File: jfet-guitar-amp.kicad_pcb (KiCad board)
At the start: 2 copper layers, 78 x 21 mm, 51 parts, among them J1 Conn_2, J2 Conn_2, J3 AudioJack4, Q1 J201, Q2 J201, Q3 J201, U1 4580, U2 TSX9291

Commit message: prepare to send to manufacture
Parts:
- R21, R22: value 4K7 -> NF
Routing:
- net Net-(C4-Pad1): track 16.2 -> 18.3 mm
- net /V_Gnd: track 88.9 -> 89.5 mm
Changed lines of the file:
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@@
-(kicad_pcb (version 20171130) (host pcbnew "(5.0.2)-1")
+(kicad_pcb (version 20171130) (host pcbnew 5.0.2-bee76a0~70~ubuntu18.04.1)
   (general
     (thickness 1.6)
     (drawings 16)
-    (tracks 185)
+    (tracks 189)
     (zones 0)
     (modules 51)
@@
   )
   (setup
-    (last_trace_width 0.5)
+    (last_trace_width 0.25)
     (user_trace_width 0.5)
     (trace_clearance 0.2)
@@
       (effects (font (size 1 1) (thickness 0.15)))
     )
-    (fp_text value 4K7 (at 0 1.65 180) (layer F.Fab)
+    (fp_text value NF (at 0 1.65 180) (layer F.Fab)
       (effects (font (size 1 1) (thickness 0.15)))
     )
@@
       (effects (font (size 1 1) (thickness 0.15)))
     )
-    (fp_text value 4K7 (at 0 1.65 180) (layer F.Fab)
+    (fp_text value NF (at 0 1.65 180) (layer F.Fab)
       (effects (font (size 1 1) (thickness 0.15)))
     )
@@
   (segment (start 112.76 94.168) (end 112.76 95.9175) (width 0.5) (layer F.Cu) (net 3))
   (segment (start 89.9645 94.615) (end 91.6455 94.615) (width 0.5) (layer F.Cu) (net 4))
-  (segment (start 96.3065 89.154) (end 103.415208 89.154) (width 0.5) (layer F.Cu) (net 4))
-  (segment (start 91.6455 93.815) (end 96.3065 89.154) (width 0.5) (layer F.Cu) (net 4))
-  (segment (start 91.6455 94.615) (end 91.6455 93.815) (width 0.5) (layer F.Cu) (net 4))
+  (segment (start 91.6455 94.615) (end 91.6455 90.2185) (width 0.5) (layer F.Cu) (net 4))
+  (segment (start 92.71 89.154) (end 103.415208 89.154) (width 0.5) (layer F.Cu) (net 4))
+  (segment (start 91.6455 90.2185) (end 92.71 89.154) (width 0.5) (layer F.Cu) (net 4))
   (segment (start 87.9575 94.483) (end 88.0895 94.615) (width 0.5) (layer F.Cu) (net 5))
   (segment (start 86.471 94.483) (end 87.9575 94.483) (width 0.5) (layer F.Cu) (net 5))
@@
   (segment (start 74.5975 89.154) (end 74.5975 91.186) (width 0.5) (layer F.Cu) (net 9))
   (segment (start 74.4705 91.313) (end 76.1515 91.313) (width 0.5) (layer F.Cu) (net 9))
-  (segment (start 87.46 102.573) (end 87.46 102.804) (width 0.25) (layer F.Cu) (net 10))
-  (segment (start 85.26 100.904) (end 85.791 100.904) (width 0.25) (layer F.Cu) (net 10))
-  (segment (start 85.791 100.904) (end 87.46 102.573) (width 0.25) (layer F.Cu) (net 10))
   (segment (start 105.1165 100.711) (end 100.3695 100.711) (width 0.5) (layer F.Cu) (net 10))
   (segment (start 100.3695 102.1955) (end 100.3695 100.711) (width 0.5) (layer F.Cu) (net 10))
@@
   (segment (start 138.811 102.489) (end 138.684 102.616) (width 0.5) (layer B.Cu) (net 10))
   (segment (start 134.874 102.616) (end 133.096 102.616) (width 0.5) (layer B.Cu) (net 10))
+  (segment (start 87.46 102.024) (end 87.46 102.804) (width 0.25) (layer F.Cu) (net 10))
+  (segment (start 86.172 100.904) (end 86.36 101.092) (width 0.25) (layer F.Cu) (net 10))
+  (segment (start 86.36 101.092) (end 86.36 101.6) (width 0.25) (layer F.Cu) (net 10))
+  (segment (start 86.36 101.6) (end 86.614 101.854) (width 0.25) (layer F.Cu) (net 10))
+  (segment (start 85.26 100.904) (end 86.172 100.904) (width 0.25) (layer F.Cu) (net 10))
+  (segment (start 86.614 101.854) (end 87.29 101.854) (width 0.25) (layer F.Cu) (net 10))
+  (segment (start 87.29 101.854) (end 87.46 102.024) (width 0.25) (layer F.Cu) (net 10))
   (segment (start 109.0145 93.218) (end 109.0145 95.25) (width 0.5) (layer F.Cu) (net 11))
   (segment (start 109.0145 93.218) (end 110.76 93.218) (width 0.5) (layer F.Cu) (net 11))

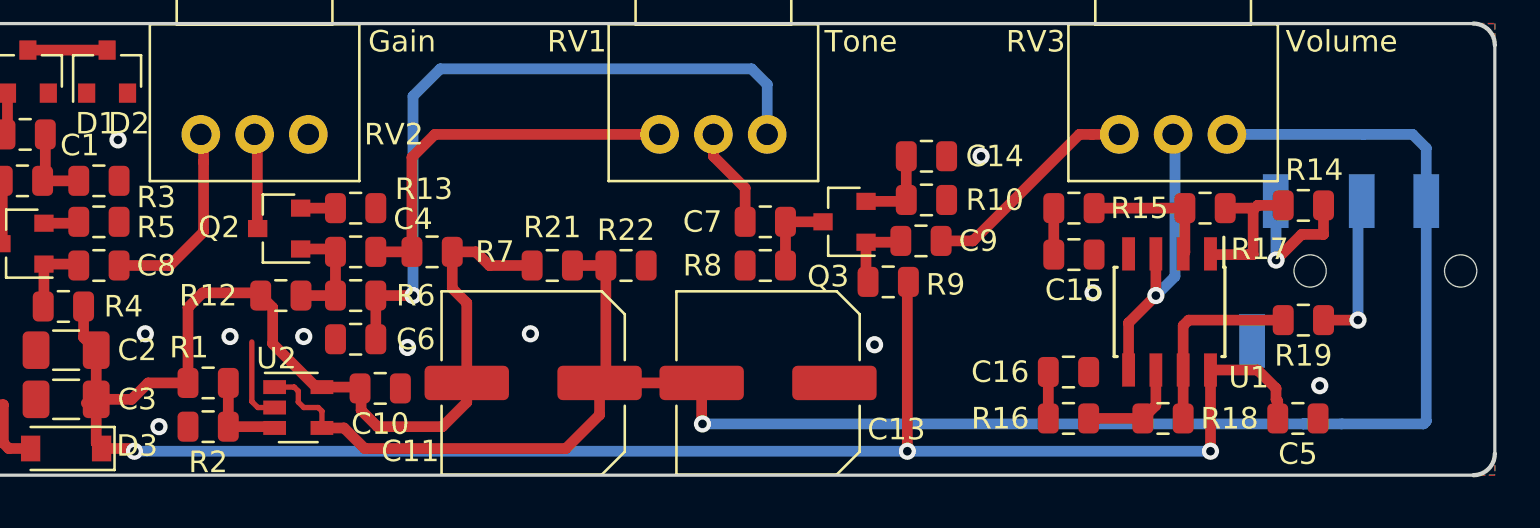
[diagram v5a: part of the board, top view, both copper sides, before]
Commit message: minor schematic changes to feedback loop and BOM, tag for prototype production
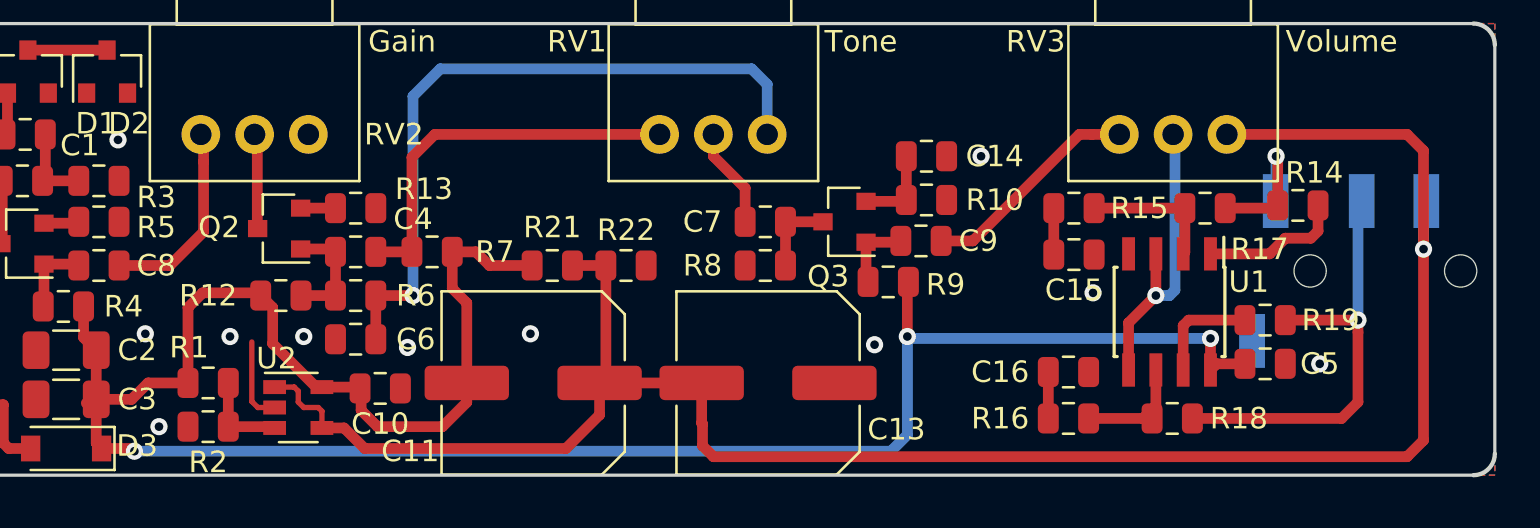
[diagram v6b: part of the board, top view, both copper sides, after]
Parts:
- C11, C13: value 470u -> NF
- moved C5 2.96 mm to (131.3, 99.8)
- moved R19 1.78 mm to (131.3, 97.8)
- moved R18 0.43 mm to (127.0, 102.4)
- moved R14 0.25 mm to (132.8, 92.5), turned to 180 degrees
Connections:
- R17 pad 1: Net-(R14-Pad1) -> Net-(J3-PadT)
- R18 pad 1: Net-(R18-Pad1) -> Net-(J3-PadR1)
- R19 pad 2: Net-(R18-Pad1) -> Net-(R19-Pad2)
- U1 pad 7: Net-(R18-Pad1) -> Net-(R19-Pad2)
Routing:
- net Net-(J3-PadR1): track 7.21 -> 20.8 mm
- net Net-(R18-Pad1): track 9.07 -> 0.00 mm
- net +9V: track 112.8 -> 107.0 mm
- net Net-(R19-Pad2): track 0.00 -> 5.04 mm
- net /V_Gnd: track 89.5 -> 93.6 mm
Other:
- board text added: "JFET guitar headphone amp Designed by Joe Earlam Rev 2"
- board text removed: "JFET guitar headphone amp Designed by Joe Earlam Rev2"

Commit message: as sent to production
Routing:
- net Net-(RV3-Pad2): track 14.2 -> 25.3 mm, vias 1 -> 0
- net Net-(C9-Pad1): track 10.3 -> 11.9 mm
- net GND: vias 12 -> 13
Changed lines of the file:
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@@
-(kicad_pcb (version 20171130) (host pcbnew 5.0.2-bee76a0~70~ubuntu16.04.1)
+(kicad_pcb (version 20171130) (host pcbnew 5.0.2-bee76a0~70~ubuntu18.04.1)
   (general
     (thickness 1.6)
     (drawings 16)
-    (tracks 195)
+    (tracks 202)
     (zones 0)
     (modules 51)
@@
       (drillshape 0)
       (scaleselection 1)
-      (outputdirectory "../../../../gerbers/jfet/"))
+      (outputdirectory "/home/joe/gerbers/jfet/"))
   )
   (net 0 "")
@@
   (via (at 79.248 98.425) (size 0.8) (drill 0.4) (layers F.Cu B.Cu) (net 8))
   (via (at 133.858 99.822) (size 0.8) (drill 0.4) (layers F.Cu B.Cu) (net 8))
+  (via (at 119.761 100.076) (size 0.8) (drill 0.4) (layers F.Cu B.Cu) (net 8))
   (segment (start 74.5975 91.186) (end 74.4705 91.313) (width 0.5) (layer F.Cu) (net 9))
   (segment (start 74.5975 89.154) (end 74.5975 91.186) (width 0.5) (layer F.Cu) (net 9))
@@
   (segment (start 72.898 103.759) (end 73.915 103.759) (width 0.5) (layer F.Cu) (net 13))
   (segment (start 72.644 103.505) (end 72.898 103.759) (width 0.5) (layer F.Cu) (net 13))
-  (segment (start 123.267208 89.154) (end 124.54 89.154) (width 0.5) (layer F.Cu) (net 14))
-  (segment (start 122.682 89.154) (end 123.267208 89.154) (width 0.5) (layer F.Cu) (net 14))
-  (segment (start 116.2535 94.107) (end 117.729 94.107) (width 0.5) (layer F.Cu) (net 14))
-  (segment (start 117.729 94.107) (end 122.682 89.154) (width 0.5) (layer F.Cu) (net 14))
+  (segment (start 118.960001 92.875999) (end 117.729 94.107) (width 0.5) (layer F.Cu) (net 14))
+  (segment (start 118.960001 90.208999) (end 118.960001 92.875999) (width 0.5) (layer F.Cu) (net 14))
+  (segment (start 117.729 94.107) (end 116.2535 94.107) (width 0.5) (layer F.Cu) (net 14))
+  (segment (start 120.015 89.154) (end 118.960001 90.208999) (width 0.5) (layer F.Cu) (net 14))
+  (segment (start 124.54 89.154) (end 120.015 89.154) (width 0.5) (layer F.Cu) (net 14))
   (segment (start 81.955 90.426792) (end 81.955 89.154) (width 0.5) (layer F.Cu) (net 15))
   (segment (start 81.955 93.686) (end 81.955 90.426792) (width 0.5) (layer F.Cu) (net 15))
@@
   (segment (start 132.2555 93.98) (end 133.447 93.98) (width 0.5) (layer F.Cu) (net 25))
   (segment (start 133.447 93.98) (end 133.7795 93.6475) (width 0.5) (layer F.Cu) (net 25))
-  (segment (start 127.508 98.044) (end 127.508 100.109) (width 0.5) (layer F.Cu) (net 32))
-  (segment (start 127.762 97.79) (end 127.508 98.044) (width 0.5) (layer F.Cu) (net 32))
   (segment (start 84.455 93.517) (end 84.471 93.533) (width 0.5) (layer F.Cu) (net 26))
   (segment (start 84.455 89.154) (end 84.455 93.517) (width 0.5) (layer F.Cu) (net 26))
@@
   (segment (start 126.238 96.647) (end 126.238 94.709) (width 0.5) (layer F.Cu) (net 27))
   (segment (start 124.968 97.917) (end 126.238 96.647) (width 0.5) (layer F.Cu) (net 27))
-  (via (at 126.238 96.647) (size 0.8) (drill 0.4) (layers F.Cu B.Cu) (net 27))
-  (segment (start 127.127 89.241) (end 127.04 89.154) (width 0.5) (layer B.Cu) (net 27))
-  (segment (start 127.127 96.393) (end 127.127 89.241) (width 0.5) (layer B.Cu) (net 27))
-  (segment (start 126.873 96.647) (end 127.127 96.393) (width 0.5) (layer B.Cu) (net 27))
-  (segment (start 126.238 96.647) (end 126.873 96.647) (width 0.5) (layer B.Cu) (net 27))
+  (segment (start 127 89.194) (end 127.04 89.154) (width 0.5) (layer F.Cu) (net 27))
+  (segment (start 127 90.678) (end 127 89.194) (width 0.5) (layer F.Cu) (net 27))
+  (segment (start 126.619 91.059) (end 127 90.678) (width 0.5) (layer F.Cu) (net 27))
+  (segment (start 124.46 97.917) (end 123.952 97.409) (width 0.5) (layer F.Cu) (net 27))
+  (segment (start 124.968 97.917) (end 124.46 97.917) (width 0.5) (layer F.Cu) (net 27))
+  (segment (start 120.396 91.059) (end 126.619 91.059) (width 0.5) (layer F.Cu) (net 27))
+  (segment (start 121.158 97.409) (end 119.888 96.139) (width 0.5) (layer F.Cu) (net 27))
+  (segment (start 123.952 97.409) (end 121.158 97.409) (width 0.5) (layer F.Cu) (net 27))
+  (segment (start 119.888 96.139) (end 119.888 91.567) (width 0.5) (layer F.Cu) (net 27))
+  (segment (start 119.888 91.567) (end 120.396 91.059) (width 0.5) (layer F.Cu) (net 27))
   (segment (start 83.1065 100.711) (end 83.1065 102.743) (width 0.5) (layer F.Cu) (net 28))
   (segment (start 85.199 102.743) (end 85.26 102.804) (width 0.5) (layer F.Cu) (net 28))
@@
   (segment (start 134.874 102.362) (end 135.636 101.6) (width 0.5) (layer F.Cu) (net 30))
   (segment (start 127.9375 102.362) (end 134.874 102.362) (width 0.5) (layer F.Cu) (net 30))
+  (segment (start 127.508 98.044) (end 127.508 100.109) (width 0.5) (layer F.Cu) (net 32))
+  (segment (start 127.762 97.79) (end 127.508 98.044) (width 0.5) (layer F.Cu) (net 32))
   (segment (start 130.3805 97.79) (end 127.762 97.79) (width 0.5) (layer F.Cu) (net 32))
   (zone (net 8) (net_name GND) (layer F.Cu) (hatch edge 0.508)

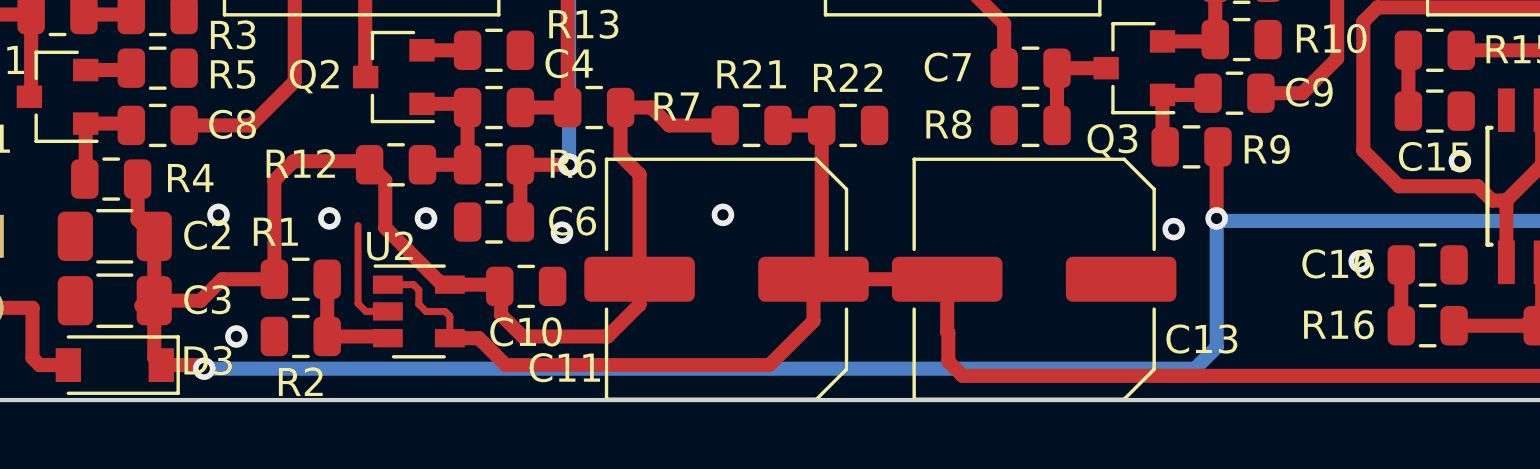
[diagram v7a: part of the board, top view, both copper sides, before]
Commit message: small tweaks: decoupling for split supply, tidied up schematic, moved via to reduce likelihood of ground loops
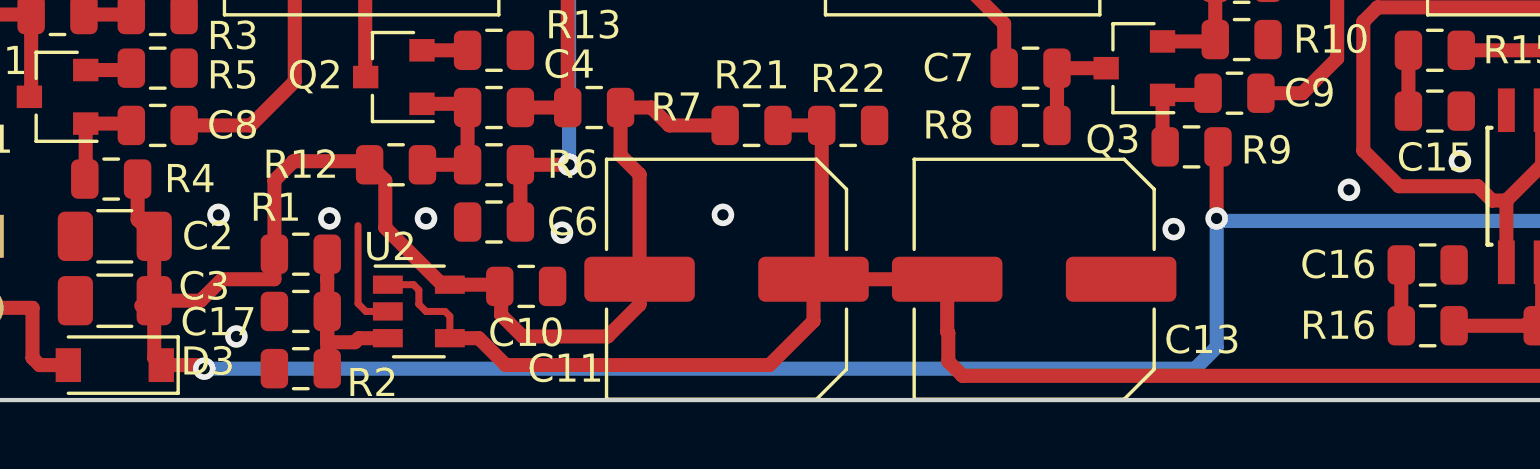
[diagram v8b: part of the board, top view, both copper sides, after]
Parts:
- added C17: 100n, Capacitor_SMD:C_0805_2012Metric, F.Cu at (82.2, 101.9)
- moved R2 1.14 mm to (82.2, 103.9)
- moved R1 0.89 mm to (82.2, 99.8)
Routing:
- net Net-(C17-Pad2): track 4.21 -> 7.25 mm
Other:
- board text added: "JFET guitar headphone amp Designed by Joe Earlam Rev 2+"
- board text removed: "JFET guitar headphone amp Designed by Joe Earlam Rev 2"
